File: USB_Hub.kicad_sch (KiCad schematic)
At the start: 47 parts, among them U4 VL822-QFN76, U5 AP7331-10WG-7, Y1 25MHz

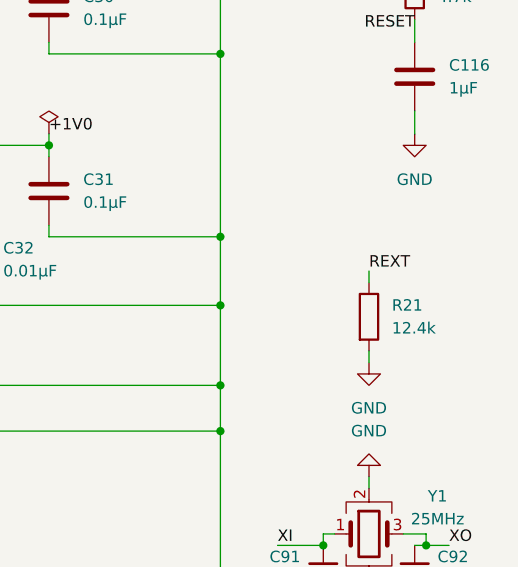
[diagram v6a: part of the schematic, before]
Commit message: Replaced 12.4k resistor with two basic parts
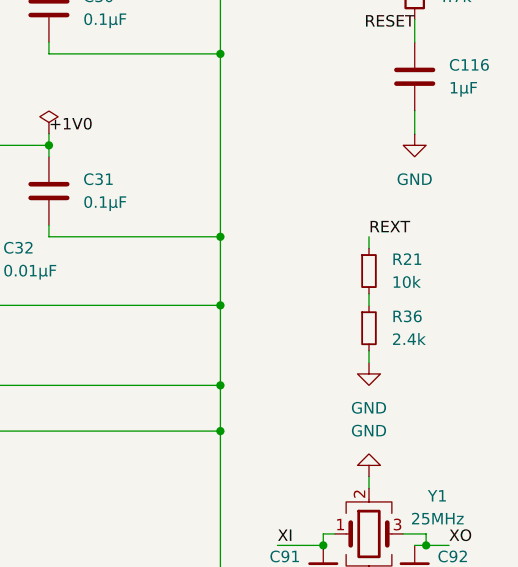
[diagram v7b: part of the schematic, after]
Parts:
- removed R21: 12.4k, Resistor_SMD:R_0805_2012Metric_Pad1.20x1.40mm_HandSolder, symbol Device:R
- added R21: 10k, Resistor_SMD:R_0402_1005Metric, symbol Device:R_Small
- added R36: 2.4k, Resistor_SMD:R_0402_1005Metric, symbol Device:R_Small
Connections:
- net GND: now also R36.2
- net REXT: now also R21.1
- new net: R21.2, R36.1
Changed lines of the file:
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@@
 	(wire
 		(pts
-			(xy 41.91 45.72) (xy 52.07 45.72)
+			(xy 261.62 99.06) (xy 261.62 100.33)
 		)
 		(stroke
@@
 	(wire
 		(pts
-			(xy 261.62 99.06) (xy 261.62 100.33)
+			(xy 41.91 45.72) (xy 52.07 45.72)
 		)
 		(stroke
@@
 	(wire
 		(pts
+			(xy 261.62 92.71) (xy 261.62 93.98)
+		)
+		(stroke
+			(width 0)
+			(type default)
+		)
+	)
+	(wire
+		(pts
 			(xy 208.28 91.44) (xy 208.28 93.98)
 		)
@@
 	(wire
 		(pts
-			(xy 261.62 90.17) (xy 261.62 91.44)
+			(xy 261.62 86.36) (xy 261.62 87.63)
 		)
 		(stroke
@@
 	)
 	(label "REXT"
-		(at 261.62 90.17 0)
+		(at 261.62 86.36 0)
 		(fields_autoplaced yes)
 		(effects
@@
 	)
 	(symbol
-		(lib_id "Device:R")
-		(at 261.62 95.25 0)
-		(unit 1)
-		(exclude_from_sim no)
-		(in_bom yes)
-		(on_board yes)
-		(dnp no)
-		(fields_autoplaced yes)
-		(property "Reference" "R21"
-			(at 264.16 93.9799 0)
-			(effects
-				(font
-					(size 1.27 1.27)
-				)
-				(justify left)
-			)
-		)
-		(property "Value" "12.4k"
-			(at 264.16 96.5199 0)
-			(effects
-				(font
-					(size 1.27 1.27)
-				)
-				(justify left)
-			)
-		)
-		(property "Footprint" "Resistor_SMD:R_0805_2012Metric_Pad1.20x1.40mm_HandSolder"
-			(at 259.842 95.25 90)
-			(effects
-				(font
-					(size 1.27 1.27)
-				)
-				(hide yes)
-			)
-		)
-		(property "Datasheet" "~"
-			(at 261.62 95.25 0)
-			(effects
-				(font
-					(size 1.27 1.27)
-				)
-				(hide yes)
-			)
-		)
-		(property "Description" "Resistor"
-			(at 261.62 95.25 0)
-			(effects
-				(font
-					(size 1.27 1.27)
-				)
-				(hide yes)
-			)
-		)
-		(property "Part_Number" "CQ05W8F1242T5E"
-			(at 261.62 95.25 0)
-			(effects
-				(font
-					(size 1.27 1.27)
-				)
-				(hide yes)
-			)
-		)
-		(property "LCSC" "C966572"
-			(at 261.62 95.25 0)
-			(effects
-				(font
-					(size 1.27 1.27)
-				)
-				(hide yes)
-			)
-		)
-		(property "Vend" ""
-			(at 261.62 95.25 0)
-			(effects
-				(font
-					(size 1.27 1.27)
-				)
-				(hide yes)
-			)
-		)
-		(property "Vendor" ""
-			(at 261.62 95.25 0)
-			(effects
-				(font
-					(size 1.27 1.27)
-				)
-				(hide yes)
-			)
-		)
-		(property "Category" ""
-			(at 261.62 95.25 0)
-			(effects
-				(font
-					(size 1.27 1.27)
-				)
-				(hide yes)
-			)
-		)
-		(property "DK_Datasheet_Link" ""
-			(at 261.62 95.25 0)
-			(effects
-				(font
-					(size 1.27 1.27)
-				)
-				(hide yes)
-			)
-		)
-		(property "DK_Detail_Page" ""
-			(at 261.62 95.25 0)
-			(effects
-				(font
-					(size 1.27 1.27)
-				)
-				(hide yes)
-			)
-		)
-		(property "Family" ""
-			(at 261.62 95.25 0)
-			(effects
-				(font
-					(size 1.27 1.27)
-				)
-				(hide yes)
-			)
-		)
-		(property "MPN" ""
-			(at 261.62 95.25 0)
-			(effects
-				(font
-					(size 1.27 1.27)
-				)
-				(hide yes)
-			)
-		)
-		(property "Manufacturer" ""
-			(at 261.62 95.25 0)
-			(effects
-				(font
-					(size 1.27 1.27)
-				)
-				(hide yes)
-			)
-		)
-		(property "Status" ""
-			(at 261.62 95.25 0)
-			(effects
-				(font
-					(size 1.27 1.27)
-				)
-				(hide yes)
-			)
-		)
-		(pin "2"
-		)
-		(pin "1"
-		)
-		(instances
-			(project "XG_Mobile_Dock"
-				(path "/f97e6956-ab08-42cb-8fed-03fa58e87f0e/ef21a87f-222f-4a81-a291-59975487be1d"
-					(reference "R21")
-					(unit 1)
-				)
-			)
-		)
-	)
-	(symbol
 		(lib_id "power:PWR_FLAG")
 		(at 226.06 74.93 0)
@@
 	)
 	(symbol
+		(lib_id "Device:R_Small")
+		(at 261.62 90.17 0)
+		(unit 1)
+		(exclude_from_sim no)
+		(in_bom yes)
+		(on_board yes)
+		(dnp no)
+		(fields_autoplaced yes)
+		(property "Reference" "R21"
+			(at 264.16 88.8999 0)
+			(effects
+				(font
+					(size 1.27 1.27)
+				)
+				(justify left)
+			)
+		)
+		(property "Value" "10k"
+			(at 264.16 91.4399 0)
+			(effects
+				(font
+					(size 1.27 1.27)
+				)
+				(justify left)
+			)
+		)
+		(property "Footprint" "Resistor_SMD:R_0402_1005Metric"
+			(at 261.62 90.17 0)
+			(effects
+				(font
+					(size 1.27 1.27)
+				)
+				(hide yes)
+			)
+		)
+		(property "Datasheet" "~"
+			(at 261.62 90.17 0)
+			(effects
+				(font
+					(size 1.27 1.27)
+				)
+				(hide yes)
+			)
+		)
+		(property "Description" "Resistor, small symbol"
+			(at 261.62 90.17 0)
+			(effects
+				(font
+					(size 1.27 1.27)
+				)
+				(hide yes)
+			)
+		)
+		(property "Part_Number" "0402WGF1002TCE"
+			(at 261.62 90.17 0)
+			(effects
+				(font
+					(size 1.27 1.27)
+				)
+				(hide yes)
+			)
+		)
+		(property "LCSC" "C25744"
+			(at 261.62 90.17 0)
+			(effects
+				(font
+					(size 1.27 1.27)
+				)
+				(hide yes)
+			)
+		)
+		(pin "2"
+		)
+		(pin "1"
+		)
+		(instances
+			(project "XG_Mobile_Dock"
+				(path "/f97e6956-ab08-42cb-8fed-03fa58e87f0e/ef21a87f-222f-4a81-a291-59975487be1d"
+					(reference "R21")
+					(unit 1)
+				)
+			)
+		)
+	)
+	(symbol
 		(lib_id "Device:C_Small")
 		(at 114.3 95.25 90)
@@
 					(unit 1)
 				)
+			)
+		)
+	)
+	(symbol
+		(lib_id "Device:R_Small")
+		(at 261.62 96.52 0)
+		(unit 1)
+		(exclude_from_sim no)
+		(in_bom yes)
+		(on_board yes)
+		(dnp no)
+		(fields_autoplaced yes)
+		(property "Reference" "R36"
+			(at 264.16 95.2499 0)
+			(effects
+				(font
+					(size 1.27 1.27)
+				)
+				(justify left)
+			)
+		)
+		(property "Value" "2.4k"
+			(at 264.16 97.7899 0)
+			(effects
+				(font
+					(size 1.27 1.27)
+				)
+				(justify left)
+			)
+		)
+		(property "Footprint" "Resistor_SMD:R_0402_1005Metric"
+			(at 261.62 96.52 0)
+			(effects
+				(font
+					(size 1.27 1.27)
+				)
+				(hide yes)
+			)
+		)
+		(property "Datasheet" "~"
+			(at 261.62 96.52 0)
+			(effects
+				(font
+					(size 1.27 1.27)
+				)
+				(hide yes)
+			)
+		)
+		(property "Description" "Resistor, small symbol"
+			(at 261.62 96.52 0)
+			(effects
+				(font
+					(size 1.27 1.27)
+				)
+				(hide yes)
+			)
+		)
+		(property "Part_Number" "0402WGF2401TCE"
+			(at 261.62 96.52 0)
+			(effects
+				(font
+					(size 1.27 1.27)
+				)
+				(hide yes)
+			)
+		)
+		(property "LCSC" "C25882"
+			(at 261.62 96.52 0)
+			(effects
+				(font
+					(size 1.27 1.27)
+				)
+				(hide yes)
+			)
+		)
+		(pin "2"
+		)
+		(pin "1"
+		)
+		(instances
+			(project "XG_Mobile_Dock"
+				(path "/f97e6956-ab08-42cb-8fed-03fa58e87f0e/ef21a87f-222f-4a81-a291-59975487be1d"
+					(reference "R36")
+					(unit 1)
+				)
